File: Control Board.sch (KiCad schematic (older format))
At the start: 19 parts, among them P1 CONN_01X12, P10 CONN_01X12, P2 CONN_01X12, P3 CONN_01X12, P4 CONN_01X12, P5 CONN_01X05, P6 CONN_01X12, P7 CONN_01X12, P8 CONN_01X05, P9 CONN_01X12, U4 RLOOP_NODE_CORE

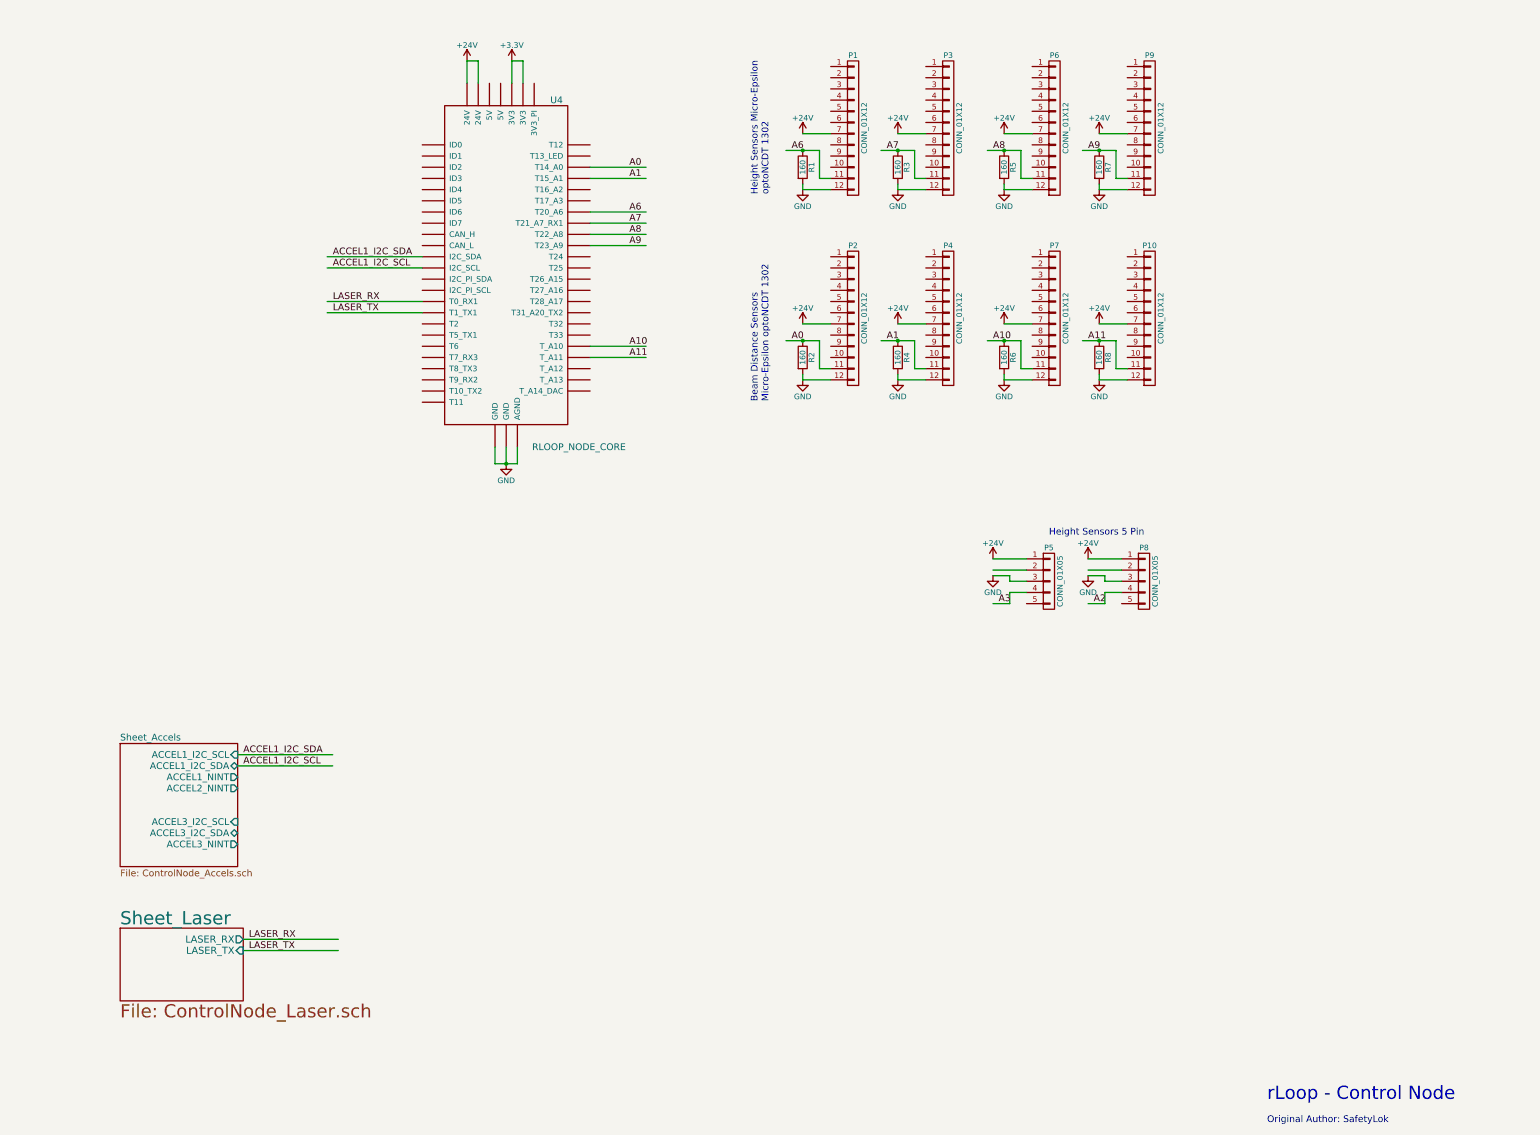
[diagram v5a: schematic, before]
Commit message: Split extra sheets out.
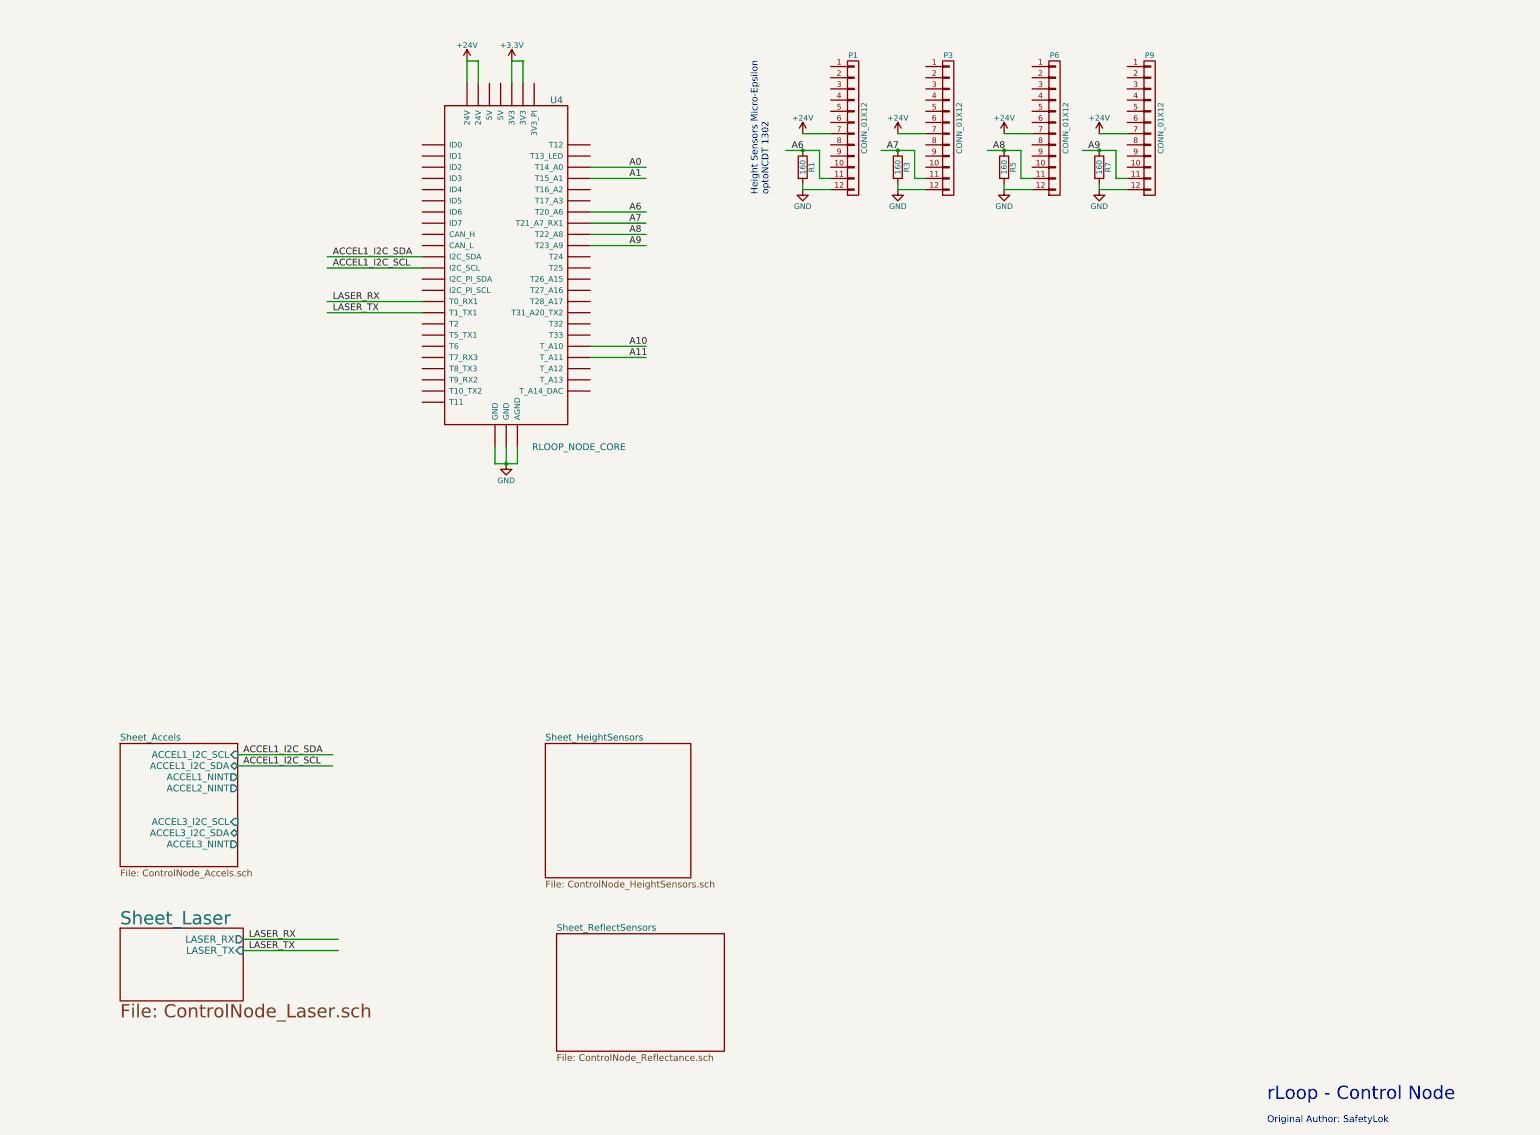
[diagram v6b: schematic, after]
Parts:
- removed P10, P2, P4, P7: CONN_01X12, symbol CONN_01X12
- removed P5, P8: CONN_01X05, symbol CONN_01X05
- removed R2, R4, R6, R8: 160, symbol R
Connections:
- net labels removed: A2, A3
- wire segments 90 -> 50
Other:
- note removed: "Beam Distance Sensors\nMicro-Epsilon optoNCDT 1302"
- note removed: "Height Sensors 5 Pin"

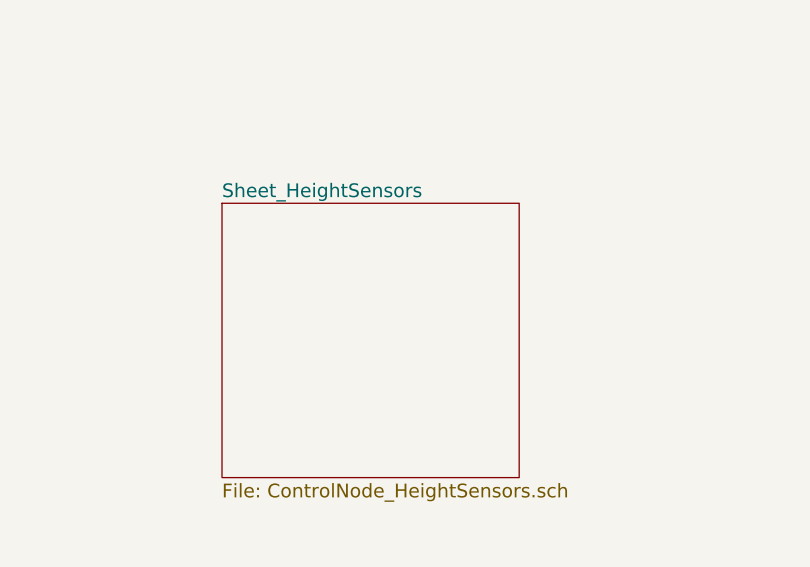
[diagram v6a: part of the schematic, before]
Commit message: Update height sensors.
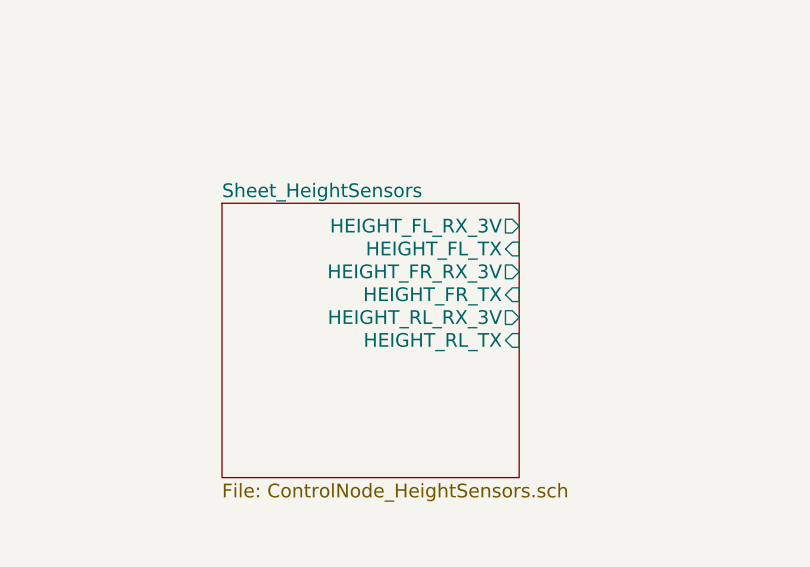
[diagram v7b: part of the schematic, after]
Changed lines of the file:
@@
 F0 "Sheet_HeightSensors" 60
 F1 "ControlNode_HeightSensors.sch" 60
+F2 "HEIGHT_FL_RX_3V" O R 6800 7100 60
+F3 "HEIGHT_FL_TX" I R 6800 7200 60
+F4 "HEIGHT_FR_RX_3V" O R 6800 7300 60
+F5 "HEIGHT_FR_TX" I R 6800 7400 60
+F6 "HEIGHT_RL_RX_3V" O R 6800 7500 60
+F7 "HEIGHT_RL_TX" I R 6800 7600 60
 $EndSheet
 $Sheet

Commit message: Release 1
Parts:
- removed P1, P3, P6, P9: CONN_01X12, symbol CONN_01X12
- removed R1, R3, R5, R7: 160, symbol R
- removed U4: RLOOP_NODE_CORE, symbol RLOOP_NODE_CORE
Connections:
- net labels added: ACCEL1_NINT, ACCEL2_NINT, ACCEL3_I2C_SCL, ACCEL3_I2C_SDA, ACCEL3_NINT, HEIGHT_FL_RX_3V, HEIGHT_FL_TX, HEIGHT_FR_RX_3V, HEIGHT_FR_TX, HEIGHT_RL_RX_3V, HEIGHT_RL_TX, LASER_NCS, LASER_NIRQ, LASER_SPI_MISO, LASER_SPI_MOSI, LASER_SPI_SCK, REFLECT_F, REFLECT_M, REFLECT_R
- net labels removed: +24V, +3.3V, A0, A1, A10, A11, A6, A7, A8, A9, GND, LASER_RX, LASER_TX
- wire segments 50 -> 42
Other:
- note removed: "Height Sensors Micro-Epsilon\noptoNCDT 1302"
